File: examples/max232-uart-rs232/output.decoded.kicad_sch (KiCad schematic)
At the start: 6 parts, among them U2 MAX232

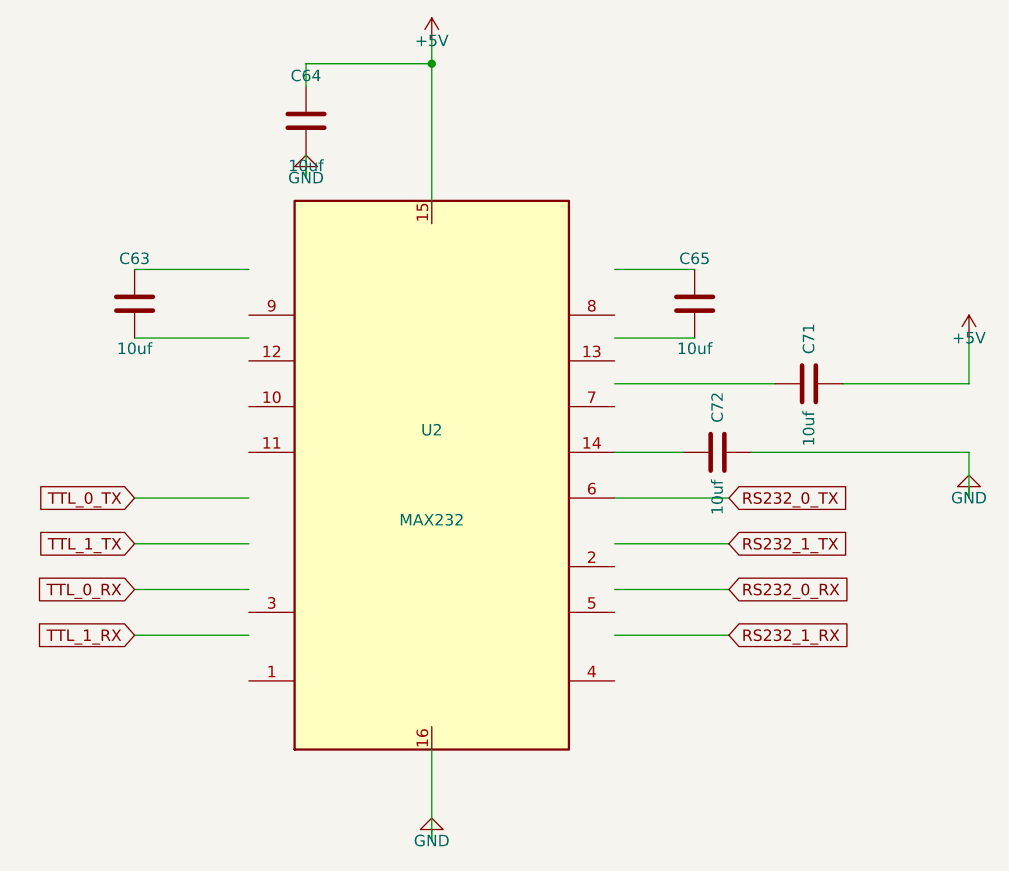
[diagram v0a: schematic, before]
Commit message: Add footprint lookup table for TOKN decoder
- Add footprints.json with comprehensive lookup table:
  - Common passive sizes (0402, 0603, 0805, etc.)
  - IC packages (SOIC, TSSOP, QFN, LQFP, etc.)
  - Specific parts (MCP2551, MAX232, ATmega, STM32, etc.)
  - Transistors, regulators, op-amps, and more

- Update tokn_decoder.py to auto-populate footprints:
  - Priority: explicit > package hint > part match > passive type
  - Handles size codes (0603) for passives automatically

Decoded schematics now have proper footprints ready for PCB layout.
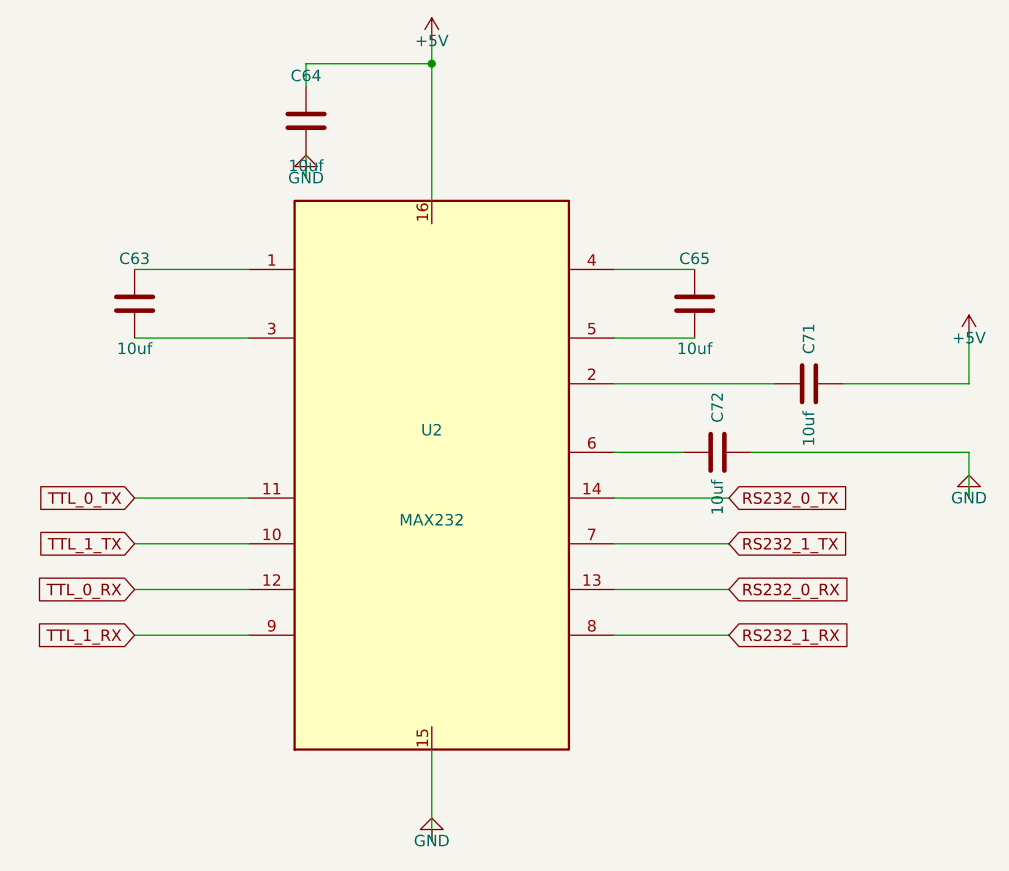
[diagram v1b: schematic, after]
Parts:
- C63, C64, C65, C71, C72: footprint (none) -> Capacitor_SMD:C_0603_1608Metric
- U2: footprint (none) -> Package_SO:SOIC-16_3.9x9.9mm_P1.27mm
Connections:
- net +5V: now also U2.16; no longer U2.15
- net GND: now also U2.15; no longer U2.16
- net RS232_0_RX: now also U2.13
- net RS232_0_TX: now also U2.14; no longer U2.6
- net RS232_1_RX: now also U2.8
- net RS232_1_TX: now also U2.7
- net TTL_0_RX: now also U2.12
- net TTL_0_TX: now also U2.11
- net TTL_1_RX: now also U2.9
- net TTL_1_TX: now also U2.10
- net at C63.1: now also U2.1
- net at C63.2: now also U2.3
- net at C72.2: now also U2.6; no longer U2.14
- net at C71.1: now also U2.2
- net at U2.4: now also C65.1
- net at U2.5: now also C65.2
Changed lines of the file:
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@@
       (at 111.76 86.28 0)
       (effects (font (size 1.27 1.27))))
-    (property "Footprint" ""
+    (property "Footprint" "Capacitor_SMD:C_0603_1608Metric"
       (at 111.76 81.28 0)
       (effects (font (size 1.27 1.27)) (hide yes)))
@@
       (at 130.81 65.96000000000001 0)
       (effects (font (size 1.27 1.27))))
-    (property "Footprint" ""
+    (property "Footprint" "Capacitor_SMD:C_0603_1608Metric"
       (at 130.81 60.96 0)
       (effects (font (size 1.27 1.27)) (hide yes)))
@@
       (at 173.99 86.28 0)
       (effects (font (size 1.27 1.27))))
-    (property "Footprint" ""
+    (property "Footprint" "Capacitor_SMD:C_0603_1608Metric"
       (at 173.99 81.28 0)
       (effects (font (size 1.27 1.27)) (hide yes)))
@@
       (at 186.69 95.17 0)
       (effects (font (size 1.27 1.27))))
-    (property "Footprint" ""
+    (property "Footprint" "Capacitor_SMD:C_0603_1608Metric"
       (at 186.69 90.17 0)
       (effects (font (size 1.27 1.27)) (hide yes)))
@@
       (at 176.53 102.79 0)
       (effects (font (size 1.27 1.27))))
-    (property "Footprint" ""
+    (property "Footprint" "Capacitor_SMD:C_0603_1608Metric"
       (at 176.53 97.79 0)
       (effects (font (size 1.27 1.27)) (hide yes)))
@@
       (at 144.78 105.33 0)
       (effects (font (size 1.27 1.27))))
-    (property "Footprint" ""
+    (property "Footprint" "Package_SO:SOIC-16_3.9x9.9mm_P1.27mm"
       (at 144.78 100.33 0)
       (effects (font (size 1.27 1.27)) (hide yes)))

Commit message: Fix decoder pin placement using TOKN pins section
- Use pin definitions from TOKN pins{REF}[N]: section instead of
  deriving positions from wire endpoints
- Calculate pin positions using standard dual-inline IC layout:
  pins 1-N/2 on left (top to bottom), N/2+1 to N on right (bottom to top)
- Include pin names from TOKN in generated lib_symbols
- Fix issue where pins with same net were merged to same position
- Regenerate all decoded schematics with correct pin placement
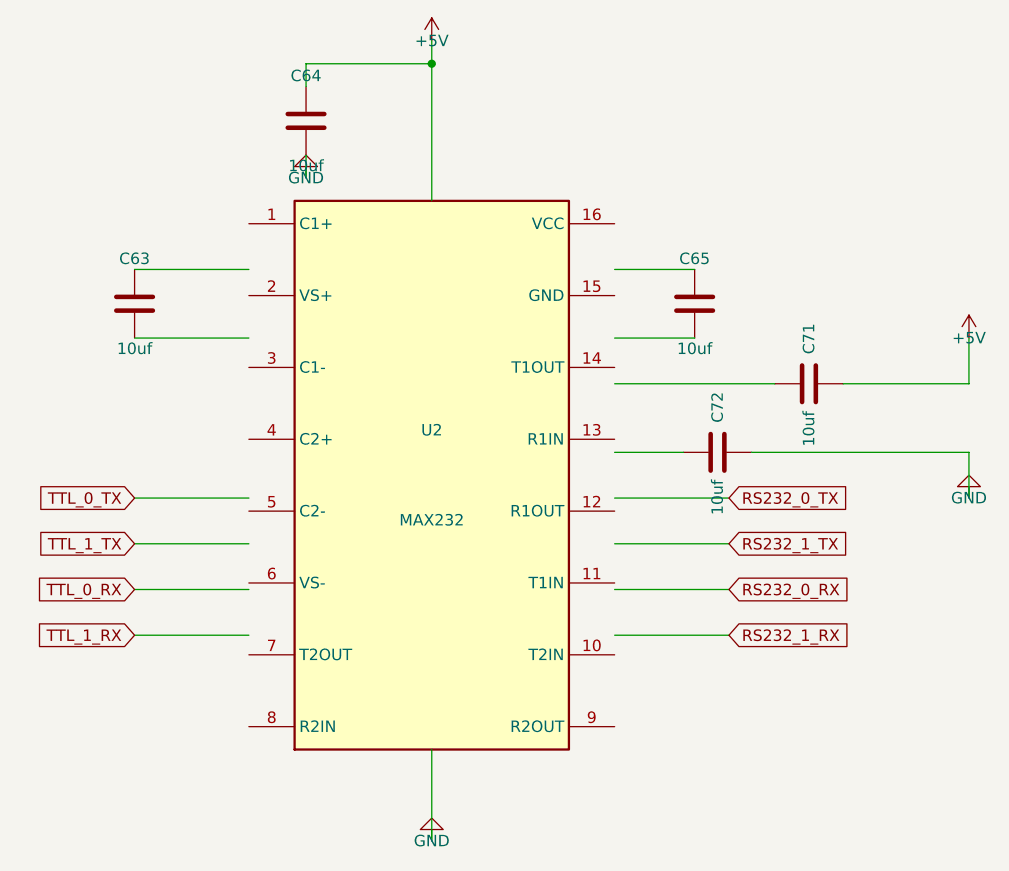
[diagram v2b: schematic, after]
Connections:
- net +5V: no longer U2.16
- net GND: no longer U2.15
- net RS232_0_RX: no longer U2.13
- net RS232_0_TX: no longer U2.14
- net RS232_1_RX: no longer U2.8
- net RS232_1_TX: no longer U2.7
- net TTL_0_RX: no longer U2.12
- net TTL_0_TX: no longer U2.11
- net TTL_1_RX: no longer U2.9
- net TTL_1_TX: no longer U2.10
- net at C63.1: no longer U2.1
- net at C63.2: no longer U2.3
- net at C72.2: no longer U2.6
- net at C71.1: no longer U2.2
- net at U2.4 (C2+): no longer C65.1
- net at U2.5 (C2-): no longer C65.2
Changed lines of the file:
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@@
       (at 144.78 100.33 0)
       (effects (font (size 1.27 1.27)) (hide yes)))
-    (pin "16"
+    (pin "1"
     )
-    (pin "15"
+    (pin "2"
+    )
+    (pin "3"
+    )
+    (pin "4"
+    )
+    (pin "5"
+    )
+    (pin "6"
+    )
+    (pin "7"
+    )
+    (pin "8"
+    )
+    (pin "9"
+    )
+    (pin "10"
+    )
+    (pin "11"
+    )
+    (pin "12"
     )
     (pin "13"
@@
     (pin "14"
     )
-    (pin "8"
+    (pin "15"
     )
-    (pin "7"
-    )
-    (pin "12"
-    )
-    (pin "11"
-    )
-    (pin "9"
-    )
-    (pin "10"
-    )
-    (pin "1"
-    )
-    (pin "2"
-    )
-    (pin "6"
-    )
-    (pin "5"
-    )
-    (pin "4"
-    )
-    (pin "3"
+    (pin "16"
     )
     (instances
